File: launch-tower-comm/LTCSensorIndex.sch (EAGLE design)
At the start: 9 parts

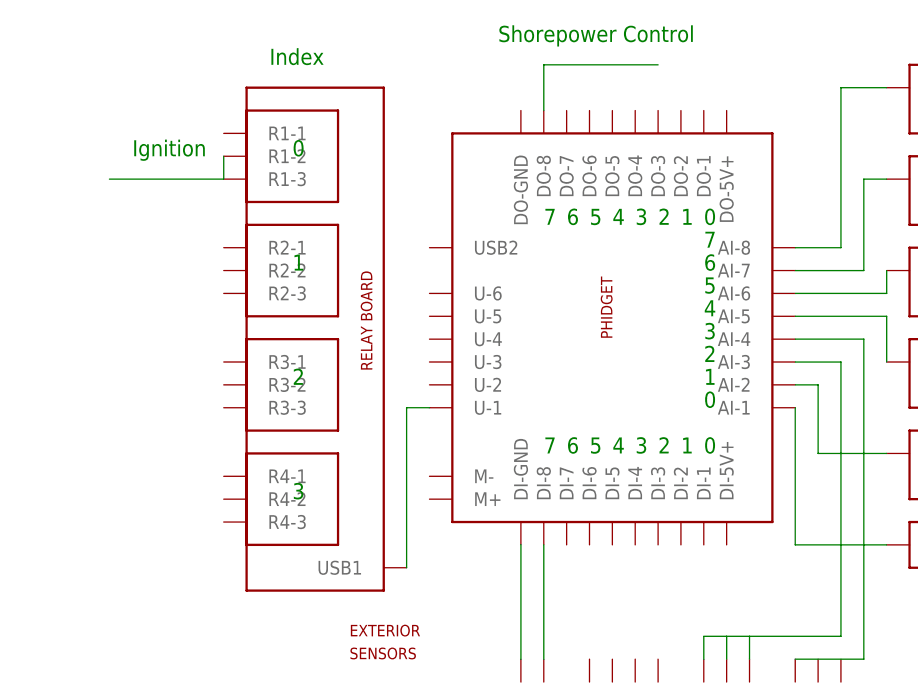
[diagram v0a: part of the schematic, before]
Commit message: Updated sensor schematic to show new shorepower relay
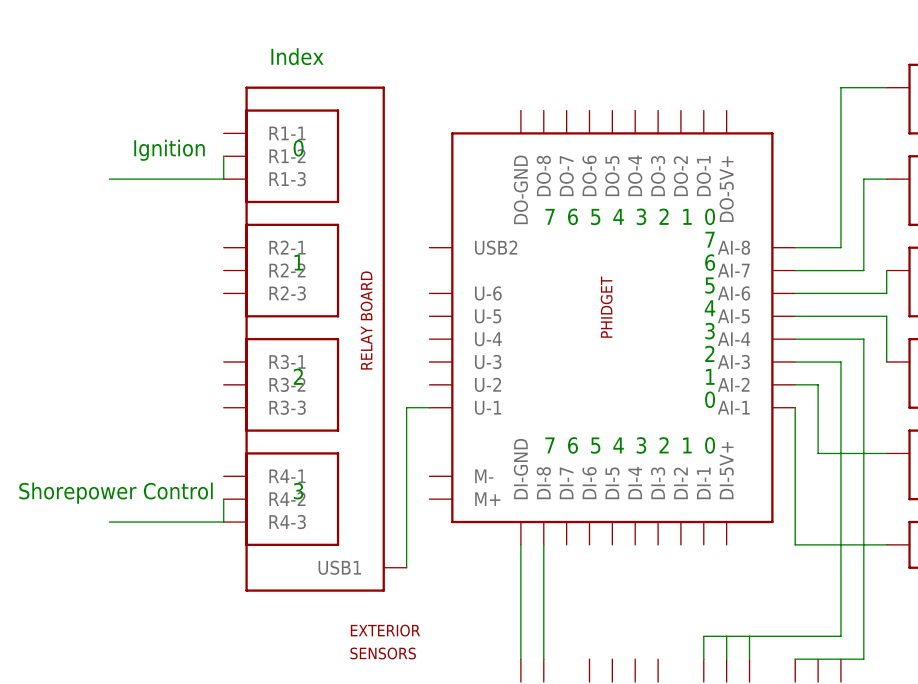
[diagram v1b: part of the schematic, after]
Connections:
- removed net SHOREPOWER_CTL: U$1.DO-8
- new net N$12: U$8.R4-2, U$8.R4-3
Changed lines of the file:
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@@
 <grid distance="0.1" unitdist="inch" unit="inch" style="lines" multiple="1" display="no" altdistance="0.01" altunitdist="inch" altunit="inch"/>
 <layers>
-<layer number="1" name="Top" color="4" fill="1" visible="yes" active="no"/>
-<layer number="16" name="Bottom" color="1" fill="1" visible="yes" active="no"/>
-<layer number="17" name="Pads" color="2" fill="1" visible="yes" active="no"/>
-<layer number="18" name="Vias" color="2" fill="1" visible="yes" active="no"/>
-<layer number="19" name="Unrouted" color="6" fill="1" visible="yes" active="no"/>
-<layer number="20" name="Dimension" color="15" fill="1" visible="yes" active="no"/>
-<layer number="21" name="tPlace" color="7" fill="1" visible="yes" active="no"/>
-<layer number="22" name="bPlace" color="7" fill="1" visible="yes" active="no"/>
-<layer number="23" name="tOrigins" color="15" fill="1" visible="yes" active="no"/>
-<layer number="24" name="bOrigins" color="15" fill="1" visible="yes" active="no"/>
-<layer number="25" name="tNames" color="7" fill="1" visible="yes" active="no"/>
-<layer number="26" name="bNames" color="7" fill="1" visible="yes" active="no"/>
-<layer number="27" name="tValues" color="7" fill="1" visible="yes" active="no"/>
-<layer number="28" name="bValues" color="7" fill="1" visible="yes" active="no"/>
+<layer number="1" name="Top" color="4" fill="1" visible="no" active="no"/>
+<layer number="16" name="Bottom" color="1" fill="1" visible="no" active="no"/>
+<layer number="17" name="Pads" color="2" fill="1" visible="no" active="no"/>
+<layer number="18" name="Vias" color="2" fill="1" visible="no" active="no"/>
+<layer number="19" name="Unrouted" color="6" fill="1" visible="no" active="no"/>
+<layer number="20" name="Dimension" color="15" fill="1" visible="no" active="no"/>
+<layer number="21" name="tPlace" color="7" fill="1" visible="no" active="no"/>
+<layer number="22" name="bPlace" color="7" fill="1" visible="no" active="no"/>
+<layer number="23" name="tOrigins" color="15" fill="1" visible="no" active="no"/>
+<layer number="24" name="bOrigins" color="15" fill="1" visible="no" active="no"/>
+<layer number="25" name="tNames" color="7" fill="1" visible="no" active="no"/>
+<layer number="26" name="bNames" color="7" fill="1" visible="no" active="no"/>
+<layer number="27" name="tValues" color="7" fill="1" visible="no" active="no"/>
+<layer number="28" name="bValues" color="7" fill="1" visible="no" active="no"/>
 <layer number="29" name="tStop" color="7" fill="3" visible="no" active="no"/>
 <layer number="30" name="bStop" color="7" fill="6" visible="no" active="no"/>
@@
 <layer number="35" name="tGlue" color="7" fill="4" visible="no" active="no"/>
 <layer number="36" name="bGlue" color="7" fill="5" visible="no" active="no"/>
-<layer number="37" name="tTest" color="7" fill="1" visible="yes" active="no"/>
-<layer number="38" name="bTest" color="7" fill="1" visible="yes" active="no"/>
+<layer number="37" name="tTest" color="7" fill="1" visible="no" active="no"/>
+<layer number="38" name="bTest" color="7" fill="1" visible="no" active="no"/>
 <layer number="39" name="tKeepout" color="4" fill="11" visible="no" active="no"/>
 <layer number="40" name="bKeepout" color="1" fill="11" visible="no" active="no"/>
@@
 <layer number="44" name="Drills" color="7" fill="1" visible="no" active="no"/>
 <layer number="45" name="Holes" color="7" fill="1" visible="no" active="no"/>
-<layer number="46" name="Milling" color="3" fill="1" visible="yes" active="no"/>
-<layer number="47" name="Measures" color="7" fill="1" visible="yes" active="no"/>
-<layer number="48" name="Document" color="7" fill="1" visible="yes" active="no"/>
-<layer number="49" name="Reference" color="7" fill="1" visible="yes" active="no"/>
-<layer number="51" name="tDocu" color="7" fill="1" visible="yes" active="no"/>
-<layer number="52" name="bDocu" color="7" fill="1" visible="yes" active="no"/>
+<layer number="46" name="Milling" color="3" fill="1" visible="no" active="no"/>
+<layer number="47" name="Measures" color="7" fill="1" visible="no" active="no"/>
+<layer number="48" name="Document" color="7" fill="1" visible="no" active="no"/>
+<layer number="49" name="Reference" color="7" fill="1" visible="no" active="no"/>
+<layer number="51" name="tDocu" color="7" fill="1" visible="no" active="no"/>
+<layer number="52" name="bDocu" color="7" fill="1" visible="no" active="no"/>
 <layer number="91" name="Nets" color="2" fill="1" visible="yes" active="yes"/>
 <layer number="92" name="Busses" color="1" fill="1" visible="yes" active="yes"/>
@@
 <text x="109.22" y="33.02" size="1.778" layer="91">Internal Temperature</text>
 <text x="10.16" y="76.2" size="1.778" layer="91">Ignition</text>
-<text x="50.8" y="88.9" size="1.778" layer="91">Shorepower Control</text>
+<text x="-2.54" y="38.1" size="1.778" layer="91">Shorepower Control</text>
 <text x="111.76" y="83.82" size="1.778" layer="91">Shorepower</text>
 <text x="111.76" y="73.66" size="1.778" layer="91">Solar</text>
@@
 </segment>
 </net>
-<net name="SHOREPOWER_CTL" class="0">
-<segment>
-<pinref part="U$1" gate="G$1" pin="DO-8"/>
-<wire x1="55.88" y1="81.28" x2="55.88" y2="86.36" width="0.1524" layer="91"/>
-<wire x1="55.88" y1="86.36" x2="68.58" y2="86.36" width="0.1524" layer="91"/>
-</segment>
-</net>
+<net name="N$12" class="0">
+<segment>
+<pinref part="U$8" gate="G$1" pin="R4-2"/>
+<pinref part="U$8" gate="G$1" pin="R4-3"/>
+<wire x1="20.32" y1="38.1" x2="20.32" y2="35.56" width="0.1524" layer="91"/>
+<wire x1="20.32" y1="35.56" x2="7.62" y2="35.56" width="0.1524" layer="91"/>
+</segment>
+</net>
